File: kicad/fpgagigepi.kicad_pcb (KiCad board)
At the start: 4 copper layers, 65 x 56 mm, 140 parts, among them J1 Conn_02x05_Odd_Even, J2 Conn_01x02, J3 OX40HAT, J4 Conn_02x05_Odd_Even, J401 Conn_01x01, J402 Conn_01x01, J403 Conn_01x01, U1 24LC32, U2 NUP4114UPXV6T1G, U3 NB3L553, U4 NUP4114UPXV6T1G, U5 NUP4114UPXV6T1G, X1 L829-1J1T-43

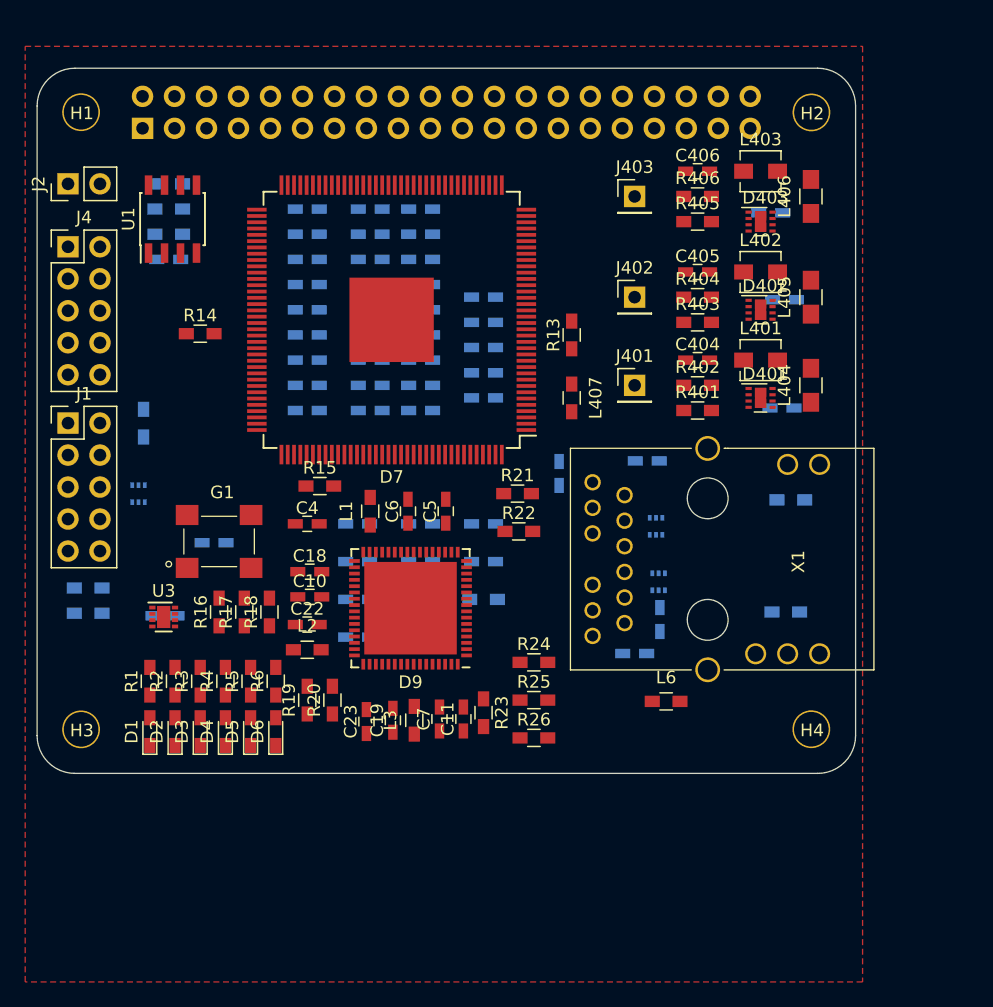
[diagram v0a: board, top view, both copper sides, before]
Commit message: Schematics updated for correct BOM generation Corrected RefDes (not renumbered yet) PCB updated (not routed) Added 3d models for new components Added folder assy (empty) Added folder bom Added BOM file (bom/BOM_fpgagigepi.xls) Added datasheet for ocscillator 25MHz (datasheets/ASEMB.pdf)
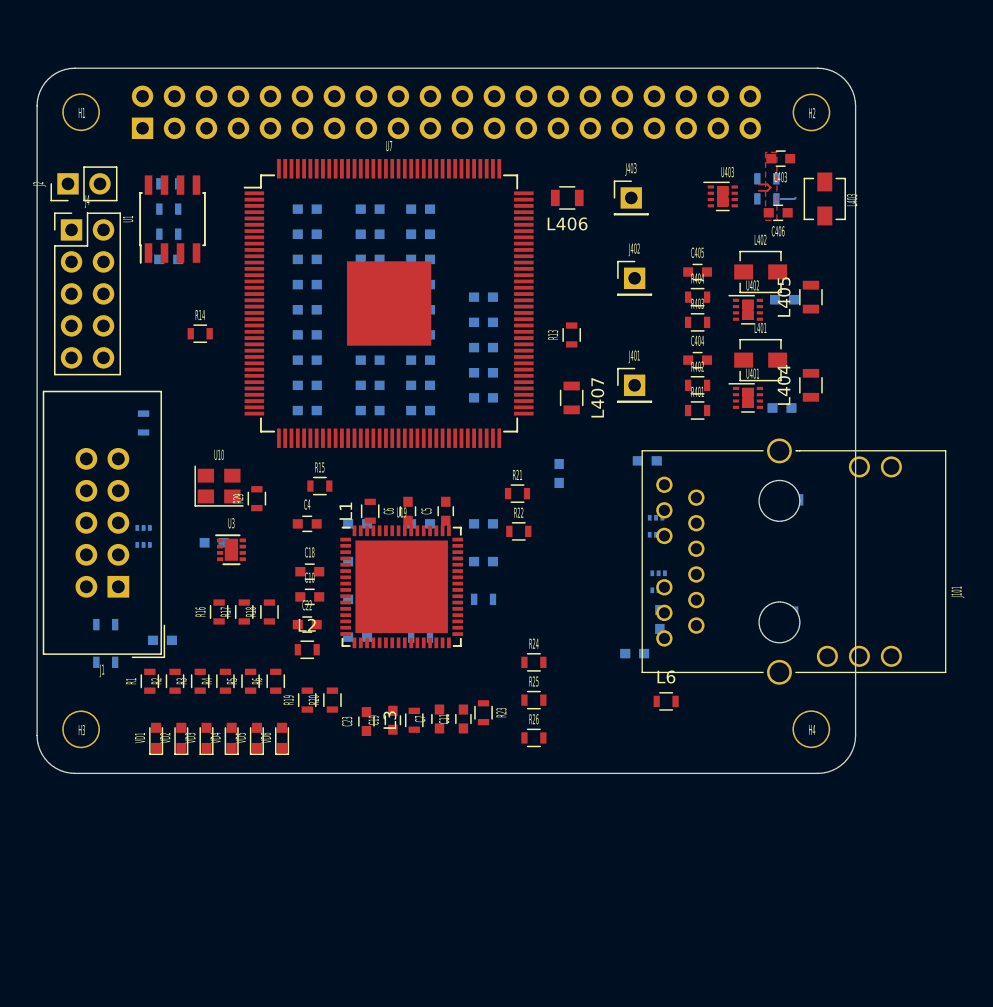
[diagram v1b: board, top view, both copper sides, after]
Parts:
- removed D1, D2, D3, D4, D5, D6: LED, LEDs:LED_0603_HandSoldering
- removed D401, D402: TLV62084, library:WSON-8_1EP_2x2mm_Pitch0.5mm
- removed D403: TLV62080, library:WSON-8_1EP_2x2mm_Pitch0.5mm
- removed D7: 10cl025, library:EQFP-144_20x20mm_Pitch0.5mm
- removed D9: KSZ9021GN, Housings_DFN_QFN:QFN-64-1EP_9x9mm_Pitch0.5mm
- removed G1: CFPS-73, library:CFPS-73
- removed X1: L829-1J1T-43, library:L829
- added J101: L829-1J1T-43, library:L829, F.Cu at (137.5, 100.0)
- added R29: 1k, Resistors_SMD:R_0603, F.Cu at (96.0, 95.0)
- added U10: ASEMB-25.000MHZ-LC-T, Oscillators:Oscillator_SMD_Abracon_ASE-4pin_3.2x2.5mm, F.Cu at (93.0, 94.0)
- added U19: KSZ9021GN, Housings_DFN_QFN:QFN-64-1EP_9x9mm_Pitch0.5mm, F.Cu at (107.5, 102.0)
- added U401: TLV62084DSGR, library:WSON-8_1EP_2x2mm_Pitch0.5mm, F.Cu at (135.0, 87.0)
- added U402: TLV62084DSGR, library:WSON-8_1EP_2x2mm_Pitch0.5mm, F.Cu at (135.0, 80.0)
- added U403: TLV62084DSGR, library:WSON-8_1EP_2x2mm_Pitch0.5mm, F.Cu at (133.0, 71.0)
- added U7: 10CL025ZE144, library:EQFP-144_20x20mm_Pitch0.5mm, F.Cu at (106.5, 79.5)
- added VD1: KP-1608SRC, LEDs:LED_0603, F.Cu at (88.0, 114.0)
- added VD2: KP-1608SGC, LEDs:LED_0603, F.Cu at (90.0, 114.0)
- added VD3: KP-1608SRC, LEDs:LED_0603, F.Cu at (92.0, 114.0)
- added VD4: KP-1608SGC, LEDs:LED_0603, F.Cu at (94.0, 114.0)
- added VD5: KP-1608SRC, LEDs:LED_0603, F.Cu at (96.0, 114.0)
- added VD6: KP-1608SGC, LEDs:LED_0603, F.Cu at (98.0, 114.0)
- C1, C10, C11, C12, C13, C14, C15, C16, C17, C18, C19, C2, C20, C21, C22, C23, C24, C25, C26, C3, C4, C401, C402, C404, C405, C406, C407, C408, C409, C410, C411, C412, C413, C414, C415, C416, C417, C418, C419, C420, C421, C422, C423, C424, C425, C426, C427, C428, C429, C430, C431, C432, C433, C434, C435, C436, C437, C438, C5, C6, C7, C8, C9: footprint Capacitors_SMD:C_0603_HandSoldering -> Capacitors_SMD:C_0603
- C403: footprint Capacitors_SMD:C_0603_HandSoldering -> Capacitors_SMD:C_0603; moved to F.Cu
- J1: value Conn_02x05_Odd_Even -> BH-10(IDC-10MS); footprint Pin_Headers:Pin_Header_Straight_2x05_Pitch2.54mm -> Connectors_IDC:IDC-Header_2x05_Pitch2.54mm_Straight
- J2: value Conn_01x02 -> PLS-2
- J3: value OX40HAT -> PBD-40(DS1023-2x20)
- J4: value Conn_02x05_Odd_Even -> PLD-10(DS1021-2x5)
- J401, J402, J403: value Conn_01x01 -> PLS-1
- L1, L2, L3, L4, L5, L6: value BLM18PG330 -> BLM18PG330SN1D; footprint Inductors_SMD:L_0603_HandSoldering -> Inductors_SMD:L_0603
- L404, L405, L406: value BLM21PG300 -> BLM21PG300SN1D; footprint Inductors_SMD:L_0805_HandSoldering -> Inductors_SMD:L_0805
- L407: value BLM18PG330 -> BLM18PG330SN1D; footprint Inductors_SMD:L_0603_HandSoldering -> Inductors_SMD:L_0805
- R1, R2, R3, R4, R5, R6: value 390 -> 390R; footprint Resistors_SMD:R_0603_HandSoldering -> Resistors_SMD:R_0603
- R10, R11, R12, R13, R14, R15, R16, R17, R18, R19, R22, R23, R24, R25, R26, R401, R402, R403, R404, R7, R8, R9: footprint Resistors_SMD:R_0603_HandSoldering -> Resistors_SMD:R_0603
- R20, R21: value 4.7k -> 4.99k 1%; footprint Resistors_SMD:R_0603_HandSoldering -> Resistors_SMD:R_0603
- R27, R28: value 220 -> 220R; footprint Resistors_SMD:R_0603_HandSoldering -> Resistors_SMD:R_0603
- R405, R406: footprint Resistors_SMD:R_0603_HandSoldering -> Resistors_SMD:R_0603; moved to B.Cu
- U1: value 24LC32 -> CAT24C32WI
- U3: value NB3L553 -> NB3L553MNR
- moved L406 19.4 mm to (120.7, 71.1), turned to 180 degrees
- moved J1 13.6 mm to (85.0, 102.0), turned to 180 degrees
- moved U3 7.58 mm to (94.0, 99.1)
- moved C406 7.20 mm to (137.4, 72.3), turned to 180 degrees
- moved R8 6.06 mm to (84.0, 108.0)
- moved R405 5.79 mm to (136.5, 71.2), turned to 180 degrees
- moved R406 5.68 mm to (136.5, 69.6), turned to 180 degrees
- moved L403 5.55 mm to (141.1, 71.2), turned to 270 degrees
- moved C403 4.37 mm to (137.6, 68.0), turned to 180 degrees
- moved U2 3.42 mm to (87.0, 98.0)
- moved C3 1.96 mm to (88.5, 106.2)
- moved R7 1.66 mm to (84.0, 105.0)
- moved J402 1.50 mm to (126.0, 77.5)
- moved J4 1.37 mm to (81.3, 73.7)
- moved J403 0.30 mm to (125.7, 71.1)
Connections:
- U4 pad 2: Net-(U4-Pad2) -> GND
- U5 pad 2: Net-(U5-Pad2) -> GND
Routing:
- net (no net): track 0.00 -> 3.35 mm
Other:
- net class Default: trace_width 0.15 -> 0.2; via_dia 0.4 -> 0.5

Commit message: Corrected path for schematics Renumbered components Remaped GMII connections to other banks PCB updated - final placement for major components and some conn routed Corrected 3d models Add text Cyclone 10LP Added 3d models for new components Added folder assy (empty) Added folder bom Added BOM file (bom/BOM_fpgagigepi.xls)
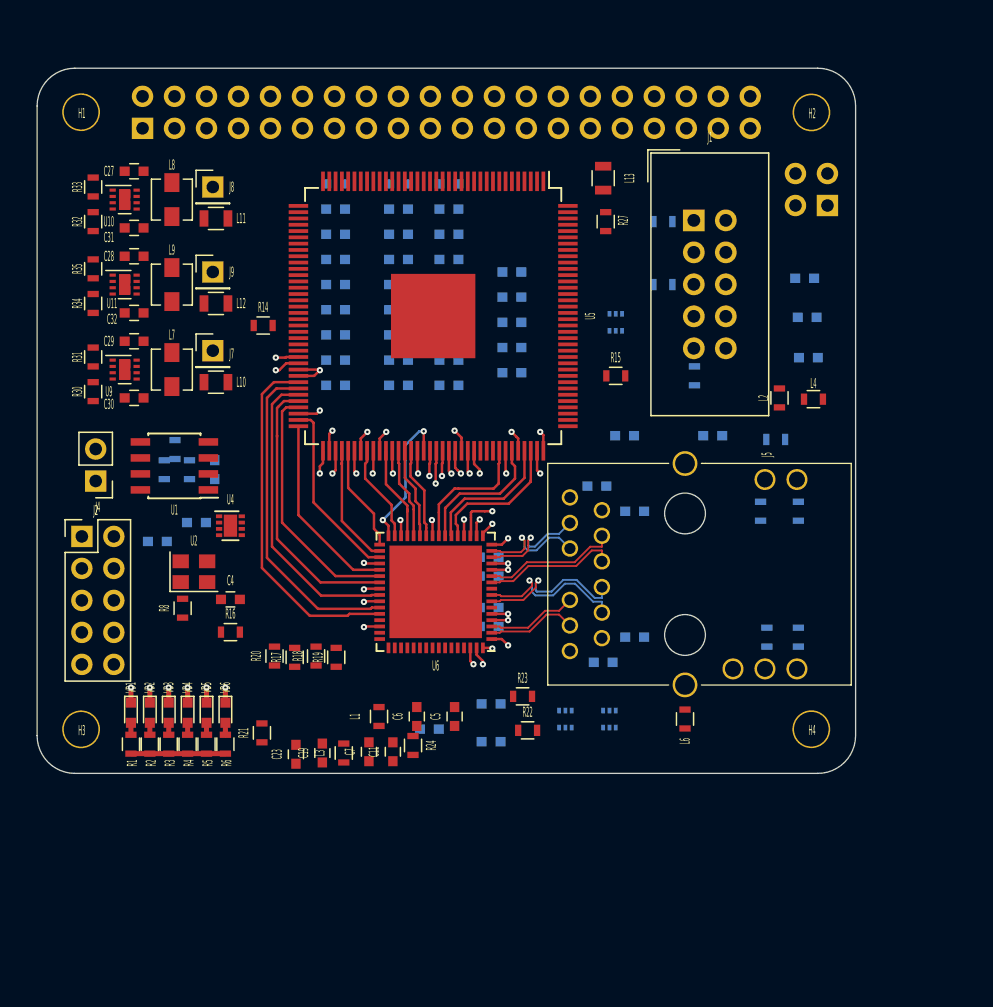
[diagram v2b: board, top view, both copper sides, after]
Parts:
- added J6: POE connector, Socket_Strips:Socket_Strip_Straight_2x02_Pitch2.54mm, B.Cu at (141.3, 71.7)
- C10, C18, C22: moved to B.Cu
- C27: renamed from C401; moved to F.Cu
- C28: renamed from C402; moved to F.Cu
- L4: moved to F.Cu
- R25: renamed from R24; moved to B.Cu
- R26: renamed from R25; moved to B.Cu
- R30: renamed from R405; moved to F.Cu
- R31: renamed from R406; moved to F.Cu
- moved R30 55.6 mm to (83.0, 86.5), turned to 90 degrees
- moved R31 55.3 mm to (83.0, 83.8), turned to 270 degrees
- moved C27 54.8 mm to (86.2, 69.0), turned to 180 degrees
- moved J1 54.2 mm to (130.7, 72.9), turned to 0 degrees
- moved L7 53.6 mm to (89.2, 84.8)
- moved R9 53.5 mm to (128.2, 78.0)
- moved C29 53.4 mm to (86.2, 82.5)
- moved C30 53.2 mm to (86.2, 87.0)
- moved U10 51.9 mm to (85.5, 71.2)
- moved C28 51.8 mm to (86.2, 75.8), turned to 180 degrees
- moved R7 50.8 mm to (130.8, 85.2), turned to 90 degrees
- moved R33 50.5 mm to (83.0, 70.2), turned to 270 degrees
- moved R32 50.3 mm to (83.0, 73.0), turned to 90 degrees
- moved U11 49.5 mm to (85.5, 78.0)
- moved U9 49.5 mm to (85.5, 84.8)
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- renumbered C403 to C29, C406 to C30, C404 to C31, C405 to C32, C407 to C33, C408 to C34, C409 to C35, C410 to C36, C411 to C37, C412 to C38, C413 to C39, C414 to C40, C415 to C41, C416 to C42, C417 to C43, C418 to C44, C419 to C45, C420 to C46, C421 to C47, C422 to C48, C423 to C49, C424 to C50, C425 to C51, C426 to C52, C427 to C53, C428 to C54, C429 to C55, C430 to C56, C431 to C57, C432 to C58, C433 to C59, C434 to C60, C435 to C61, C436 to C62, C437 to C63, C438 to C64, J101 to J5, J403 to J7, J401 to J8, J402 to J9, L406 to L10, L404 to L11, L405 to L12, L407 to L13, L403 to L7, L401 to L8, L402 to L9, R9 to R10, R10 to R11, R11 to R12, R12 to R13, R13 to R15, R15 to R16, R16 to R17, R17 to R18, R18 to R19, R19 to R20, R20 to R21, R21 to R22, R22 to R23, R23 to R24, R26 to R27, R27 to R28, R28 to R29, R401 to R32, R402 to R33, R403 to R34, R404 to R35, R29 to R8, R8 to R9, U401 to U10, U402 to U11, U10 to U2, U2 to U3, U3 to U4, U7 to U5, U19 to U6, U4 to U7, U5 to U8, U403 to U9
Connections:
- net /ethernet.sch/TXRXM_A renamed /ethernet.sch/TXRXA-
- net /ethernet.sch/TXRXM_B renamed /ethernet.sch/TXRXB-
- net /ethernet.sch/TXRXM_C renamed /ethernet.sch/TXRXC-
- net /ethernet.sch/TXRXM_D renamed /ethernet.sch/TXRXD-
- net /ethernet.sch/TXRXP_A renamed /ethernet.sch/TXRXA+
- net /ethernet.sch/TXRXP_B renamed /ethernet.sch/TXRXB+
- net /ethernet.sch/TXRXP_C renamed /ethernet.sch/TXRXC+
- net /ethernet.sch/TXRXP_D renamed /ethernet.sch/TXRXD+
- U5 pad 101: Net-(U7-Pad101) -> TXD3
- U5 pad 103: Net-(U7-Pad103) -> TXD2
- U5 pad 105: USER_LED2 -> TXD1
- U5 pad 106: USER_LED3 -> TXD0
- U5 pad 111: /ethernet.sch/RXD0 -> Net-(U5-Pad111)
- U5 pad 112: /ethernet.sch/RXD1 -> IO_76
- U5 pad 113: /ethernet.sch/RXD2 -> IO_77
- U5 pad 114: /ethernet.sch/RXD3 -> IO_80
- U5 pad 115: /ethernet.sch/RXD4 -> IO_83
- U5 pad 119: /ethernet.sch/RXD5 -> IO_85
- U5 pad 120: /ethernet.sch/RXD6 -> IO_86
- U5 pad 121: /ethernet.sch/RXD7 -> IO_87
- U5 pad 125: /ethernet.sch/RX_CLK -> Net-(U5-Pad125)
- U5 pad 132: /ethernet.sch/TX_ER -> Net-(U5-Pad132)
- U5 pad 133: /ethernet.sch/TX_EN -> Net-(U5-Pad133)
- U5 pad 54: CLK_125M -> Net-(U5-Pad54)
- U5 pad 55: 25M_A -> /ethernet.sch/RX_CLK
- U5 pad 58: /ethernet.sch/TXD0 -> Net-(U5-Pad58)
- U5 pad 59: /ethernet.sch/TXD1 -> Net-(U5-Pad59)
- U5 pad 60: /ethernet.sch/TXD2 -> Net-(U5-Pad60)
- U5 pad 65: /ethernet.sch/TXD3 -> /ethernet.sch/RXD0
- U5 pad 66: /ethernet.sch/TXD4 -> /ethernet.sch/RXD1
- U5 pad 67: /ethernet.sch/TXD5 -> /ethernet.sch/RXD2
- U5 pad 68: /ethernet.sch/TXD6 -> /ethernet.sch/RXD3
- U5 pad 69: /ethernet.sch/TXD7 -> /ethernet.sch/RXD4
- U5 pad 71: /ethernet.sch/TX_CLK -> /ethernet.sch/RXD6
- U5 pad 72: /ethernet.sch/GTX_CLK -> /ethernet.sch/RXD5
- U5 pad 76: IO_76 -> /ethernet.sch/RXD7
- U5 pad 77: IO_77 -> /ethernet.sch/TX_EN
- U5 pad 80: IO_80 -> /ethernet.sch/TX_ER
- U5 pad 83: IO_83 -> /ethernet.sch/TXD7
- U5 pad 85: IO_85 -> /ethernet.sch/TXD6
- U5 pad 86: IO_86 -> /ethernet.sch/TXD5
- U5 pad 87: IO_87 -> /ethernet.sch/TXD4
- U5 pad 88: GND -> /ethernet.sch/TX_CLK
- U5 pad 89: GND -> /ethernet.sch/GTX_CLK
- U5 pad 98: IO_98 -> Net-(U5-Pad98)
- U5 pad 99: IO_99 -> Net-(U5-Pad99)
- U6 pad 21: /ethernet.sch/TXD0 -> TXD0
- U6 pad 22: /ethernet.sch/TXD1 -> TXD1
- U6 pad 23: /ethernet.sch/TXD2 -> TXD2
- U6 pad 24: /ethernet.sch/TXD3 -> TXD3
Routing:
- net GND: track 0.00 -> 29.7 mm, vias 0 -> 14
- net /ethernet.sch/RXD0: track 0.00 -> 28.1 mm
- net /ethernet.sch/RXD1: track 0.00 -> 26.2 mm
- net /ethernet.sch/RXD2: track 0.00 -> 23.9 mm
- net /ethernet.sch/RXD3: track 0.00 -> 22.0 mm
- net /ethernet.sch/RXD4: track 0.00 -> 19.8 mm
- net /ethernet.sch/RXD5: track 0.00 -> 15.3 mm
- net /ethernet.sch/RXD6: track 0.00 -> 14.7 mm
- net +3V3: track 0.00 -> 13.2 mm, vias 0 -> 3
- net /ethernet.sch/TXRXB+: track 0.00 -> 12.6 mm, vias 0 -> 1
- net /ethernet.sch/TXRXB-: track 0.00 -> 12.6 mm, vias 0 -> 1
- net /ethernet.sch/GTX_CLK: track 0.00 -> 11.6 mm, vias 0 -> 2
- net TXD0: track 0.00 -> 11.2 mm
- net TXD2: track 0.00 -> 11.1 mm
- net TXD1: track 0.00 -> 11.0 mm
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- removed copper zone on F.Cu, net GND
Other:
- net class Default: clearance 0.2 -> 0.15
- rule trace_clearance: 0.2 -> 0.15
